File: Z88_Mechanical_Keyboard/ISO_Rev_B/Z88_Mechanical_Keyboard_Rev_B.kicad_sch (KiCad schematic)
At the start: 72 parts, among them SW1 SHIFT_RH, SW10 SHIFT_LH, SW11 SPACE, SW12 VASEN, SW13 OIKEIN, SW14 ALAS, SW15 YLÖS, SW16 ENTER, SW17 ESC, SW18 TAB, SW19 YKSI, SW2 APUA!, SW20 KAKSI, SW21 KOLME, SW22 NELJÄ, SW23 VIISI, SW24 KUUSI, SW25 INDEX, SW26 DIAMOND, SW27 Q, SW28 W, SW29 E, SW3 [, SW30 R, SW31 T, SW32 Y, SW33 CAPS_LOCK, SW34 MENU, SW35 A, SW36 S, SW37 D, SW38 F, SW39 G, SW4 ], SW40 H, SW41 DOT, SW42 COMMA, SW43 Z, SW44 X, SW45 C, SW46 V, SW47 B, SW48 N, SW49 /FORWSLASH/, SW5 UNDERSCORE, SW50 SEMICOLON, SW51 L, SW52 M, SW53 K, SW54 J, SW55 U, SW56 SEITSEMÄN, SW57 GBP, SW58 DOUBLE_QUOTE, SW59 NOLLA, SW6 EQUALS, SW60 P, SW61 YHDEKSÄN, SW62 O, SW63 I, SW64 KAHDEKSAN, SW7 \BACKSLASH\, SW8 DELETE, SW9 SQUARE

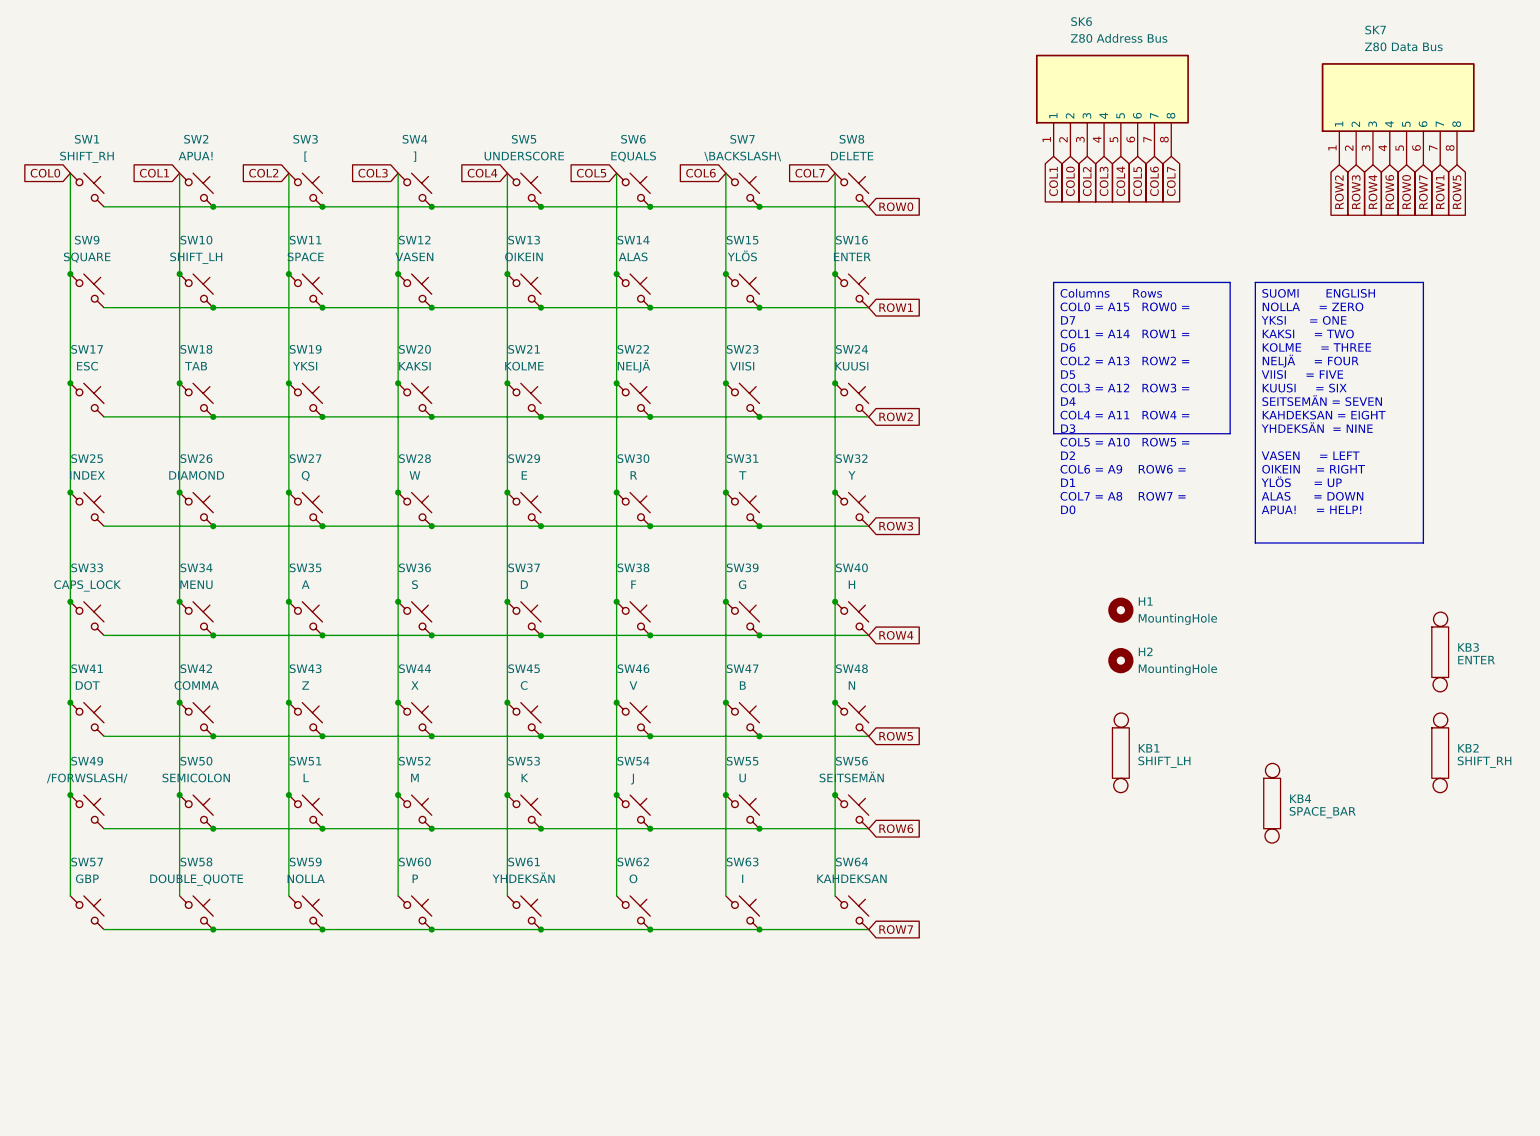
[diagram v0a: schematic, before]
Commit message: Updated ISO Rev. B, removed obsolete designs
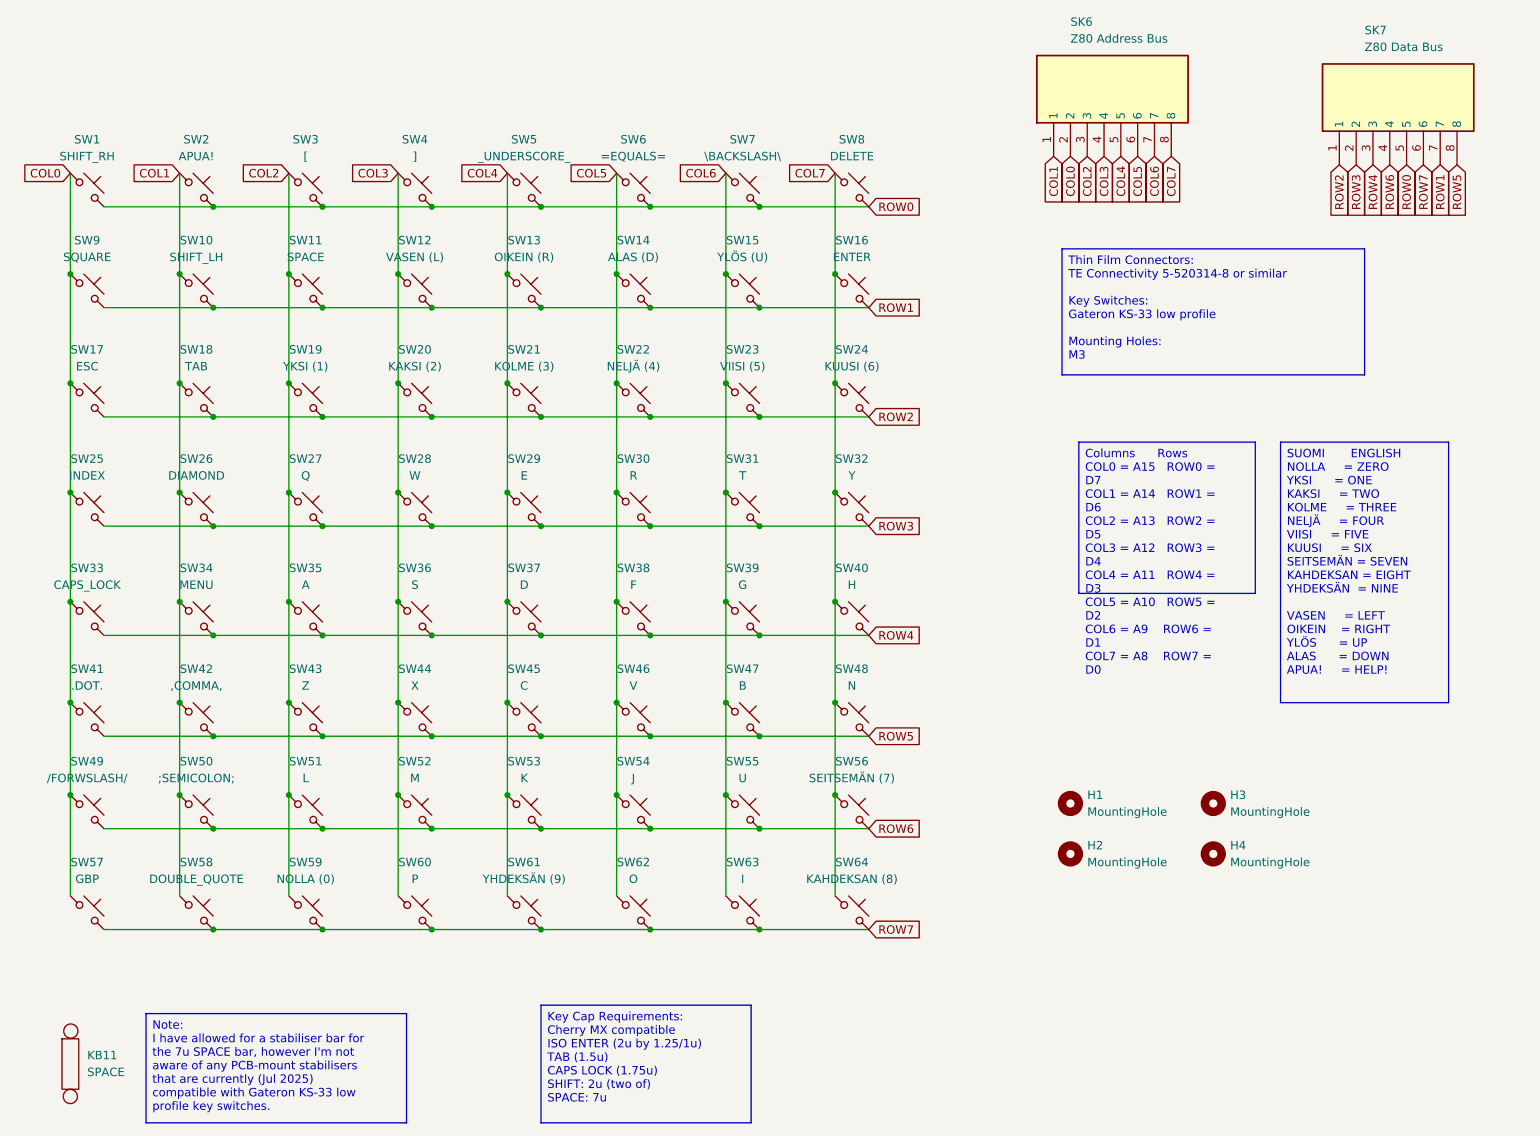
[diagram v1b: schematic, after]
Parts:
- removed KB1: SHIFT_LH, PCM_Mounting_Keyboard_Stabilizer:Stabilizer_Cherry_MX_2.00u, symbol Clueless_Engineer:Stabiliser
- removed KB2: SHIFT_RH, PCM_Mounting_Keyboard_Stabilizer:Stabilizer_Cherry_MX_2.00u, symbol Clueless_Engineer:Stabiliser
- removed KB3: ENTER, PCM_Mounting_Keyboard_Stabilizer:Stabilizer_Cherry_MX_2.00u, symbol Clueless_Engineer:Stabiliser
- removed KB4: SPACE_BAR, PCM_Mounting_Keyboard_Stabilizer:Stabilizer_Cherry_MX_7.00u, symbol Clueless_Engineer:Stabiliser
- added H3, H4: MountingHole, MountingHole:MountingHole_3.2mm_M3, symbol Mechanical:MountingHole
- added KB11: SPACE, PCM_Mounting_Keyboard_Stabilizer:Stabilizer_Cherry_MX_7.00u, symbol Clueless_Engineer:Stabiliser
- SW12: value VASEN -> VASEN (L)
- SW13: value OIKEIN -> OIKEIN (R)
- SW14: value ALAS -> ALAS (D)
- SW15: value YLÖS -> YLÖS (U)
- SW19: value YKSI -> YKSI (1)
- SW20: value KAKSI -> KAKSI (2)
- SW21: value KOLME -> KOLME (3)
- SW22: value NELJÄ -> NELJÄ (4)
- SW23: value VIISI -> VIISI (5)
- SW24: value KUUSI -> KUUSI (6)
- SW41: value DOT -> .DOT.
- SW42: value COMMA -> ,COMMA,
- SW5: value UNDERSCORE -> _UNDERSCORE_
- SW50: value SEMICOLON -> ;SEMICOLON;
- SW56: value SEITSEMÄN -> SEITSEMÄN (7)
- SW59: value NOLLA -> NOLLA (0)
- SW6: value EQUALS -> =EQUALS=
- SW61: value YHDEKSÄN -> YHDEKSÄN (9)
- SW64: value KAHDEKSAN -> KAHDEKSAN (8)
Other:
- moved on the sheet: H1, H2
